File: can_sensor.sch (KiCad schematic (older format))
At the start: 53 parts, among them J1 TEST_1P, J2 TEST_1P, J3 TEST_1P, J4 TEST_1P, P1 IO1, P2 IO2, P4 CONN_01X03, P5 USB, P6 CAN_IN, P7 CAN_OUT, P8 TERM, Q1 Q_PMOS_GSD, SW1 RESET, SW2 BOOT, U1 NJM2870F0, U2 MIC5317, U3 STM32F042C6, U4 mcp2562

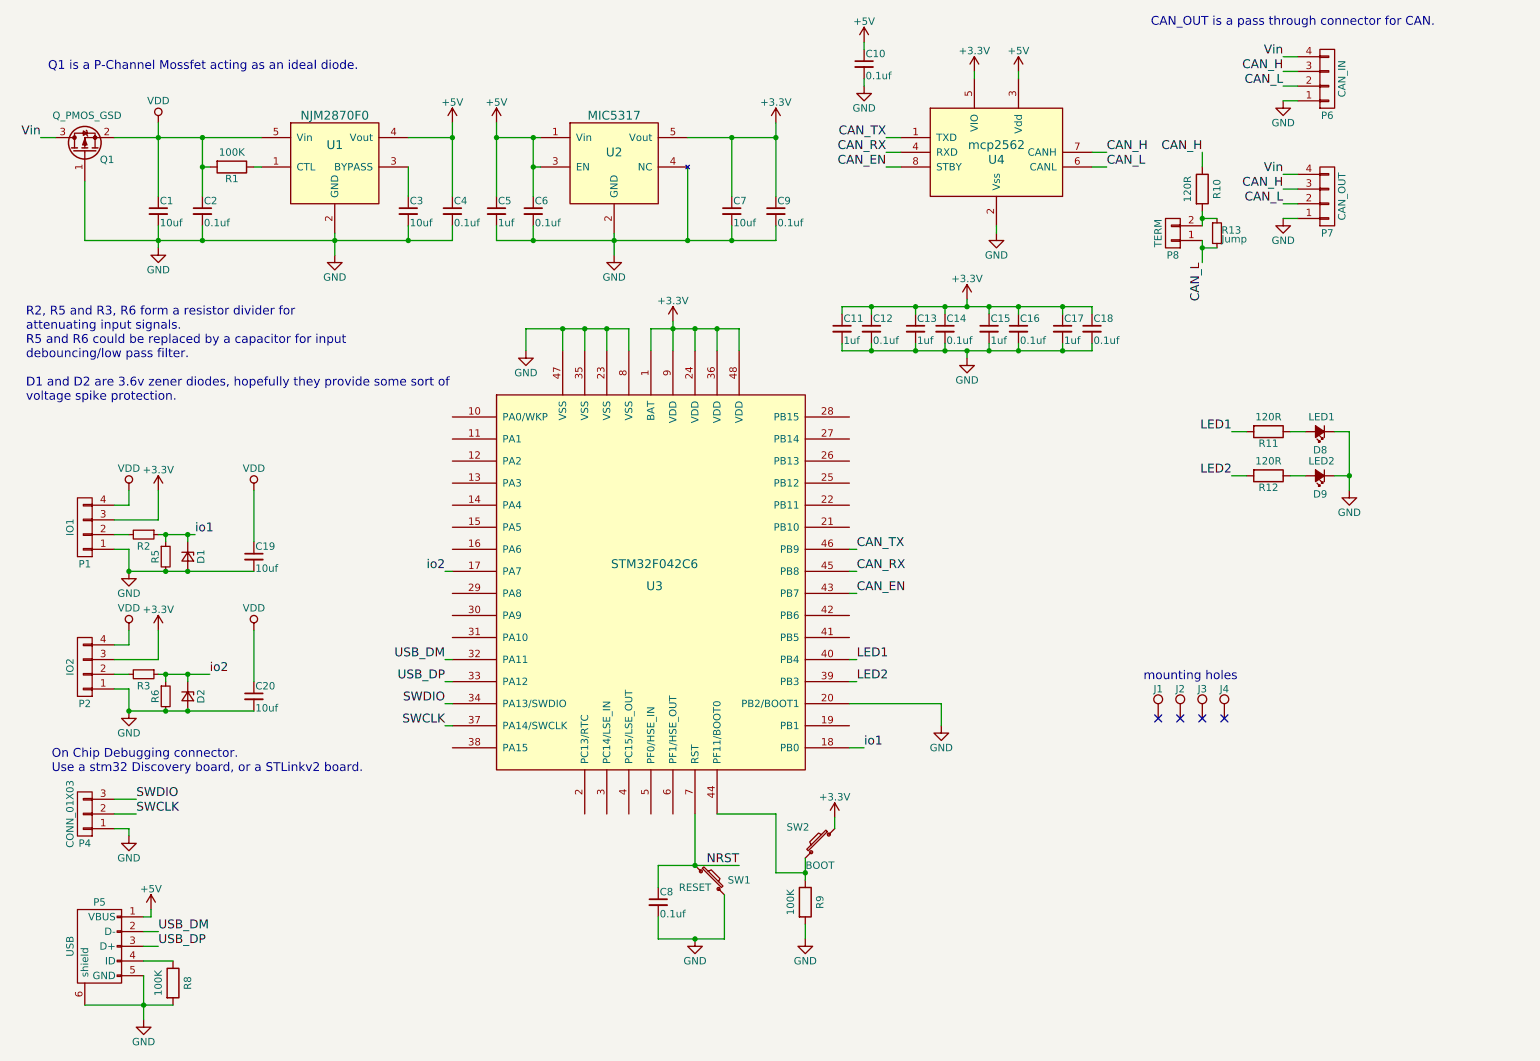
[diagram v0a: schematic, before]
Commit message: Added SPI and I2C connectors to the schematic
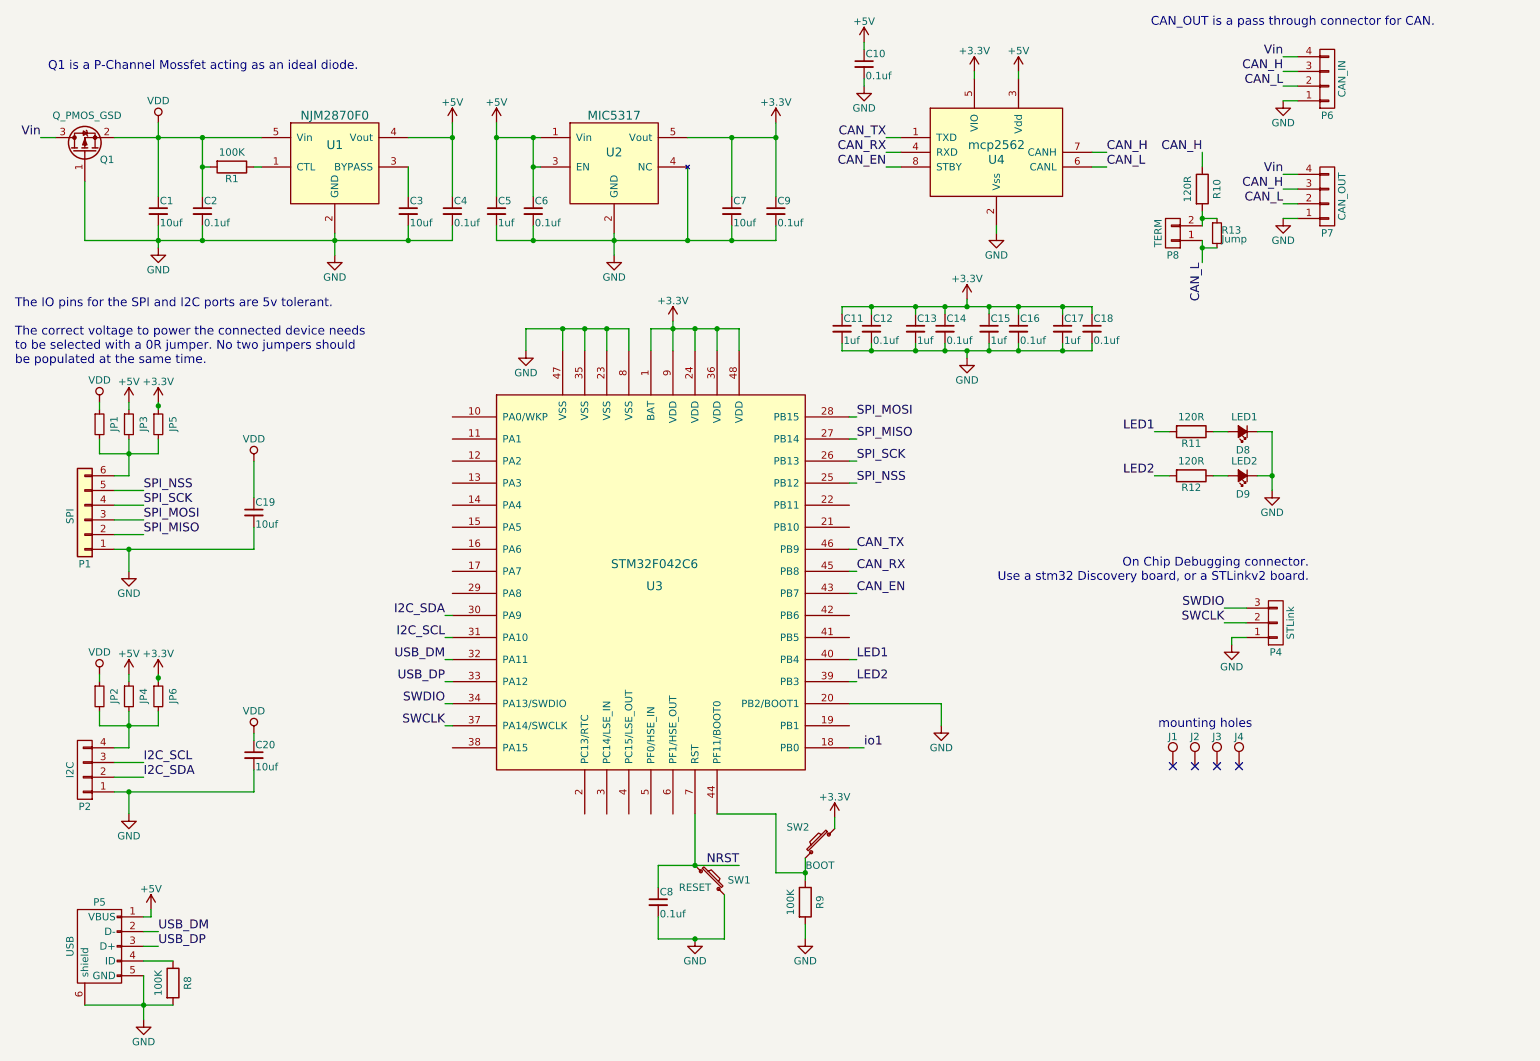
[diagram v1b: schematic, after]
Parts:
- removed D1, D2: D_Zener_Small, Diodes_SMD:D_SOD-123, symbol D_Zener_Small
- removed P1: IO1, User_Connectors:Molex-duraClick-4conn, symbol CONN_01X04
- removed R2, R3, R5, R6: R, Resistors_SMD:R_0603_HandSoldering, symbol R_Small
- added JP1, JP2: Vin, symbol R_Small
- added JP3, JP4: 3V, symbol R_Small
- added JP5, JP6: 5V, symbol R_Small
- added P1: SPI, symbol Conn_01x06
- P2: value IO2 -> I2C
- P4: value CONN_01X03 -> STLink
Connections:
- net +3V3: now also JP5.1, JP6.1; no longer P2.3 (P3)
- net +5V: now also JP3.1, JP4.1
- net GND: now also P1.1 (Pin_1)
- net VDD: now also JP1.1, JP2.1; no longer P2.4 (P4)
- net I2C_SDA: now reaches P2.2 (P2)
- net I2C_SDA: now also U3.30 (PA9)
- net SPI_NSS: now reaches U3.25 (PB12)
- net SPI_NSS: now also P1.5 (Pin_5)
- net SPI_SCK: now reaches U3.26 (PB13)
- net SPI_SCK: now also P1.4 (Pin_4)
- net SPI_MISO: now reaches U3.27 (PB14)
- net SPI_MISO: now also P1.2 (Pin_2)
- net SPI_MOSI: now reaches U3.28 (PB15)
- net SPI_MOSI: now also P1.3 (Pin_3)
- net I2C_SCL: now reaches U3.31 (PA10)
- net I2C_SCL: now also P2.3 (P3)
- net io2: no longer names the net of U3.17 (PA7)
- new net: JP2.2, JP4.2, JP6.2, P2.4 (P4)
- new net: JP1.2, JP3.2, JP5.2, P1.6 (Pin_6)
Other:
- note added: "The IO pins for the SPI and I2C ports are 5v tolerant.\n\nThe correct voltage to power the connected device needs \nto be selected with a 0R jumper. No two jumpers should \nbe populated at the same time."
- note removed: "R2, R5 and R3, R6 form a resistor divider for \nattenuating input signals.\nR5 and R6 could be replaced by a capacitor for input \ndebouncing/low pass filter.\n\nD1 and D2 are 3.6v zener diodes, hopefully they provide some sort of \nvoltage spike protection."
- moved on the sheet: C19, C20, D8, D9, J1, J2, J3, J4, P2, P4, R11, R12

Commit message: Added footprints to most components
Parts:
- D8, D9: footprint LEDs:LED_0603 -> LEDs:LED_0603_HandSoldering
- J1, J2, J3, J4: footprint (none) -> Mounting_Holes:MountingHole_3.2mm_M3_ISO7380_Pad
- JP1, JP2, JP3, JP4, JP5, JP6: footprint (none) -> Resistors_SMD:R_0603_HandSoldering

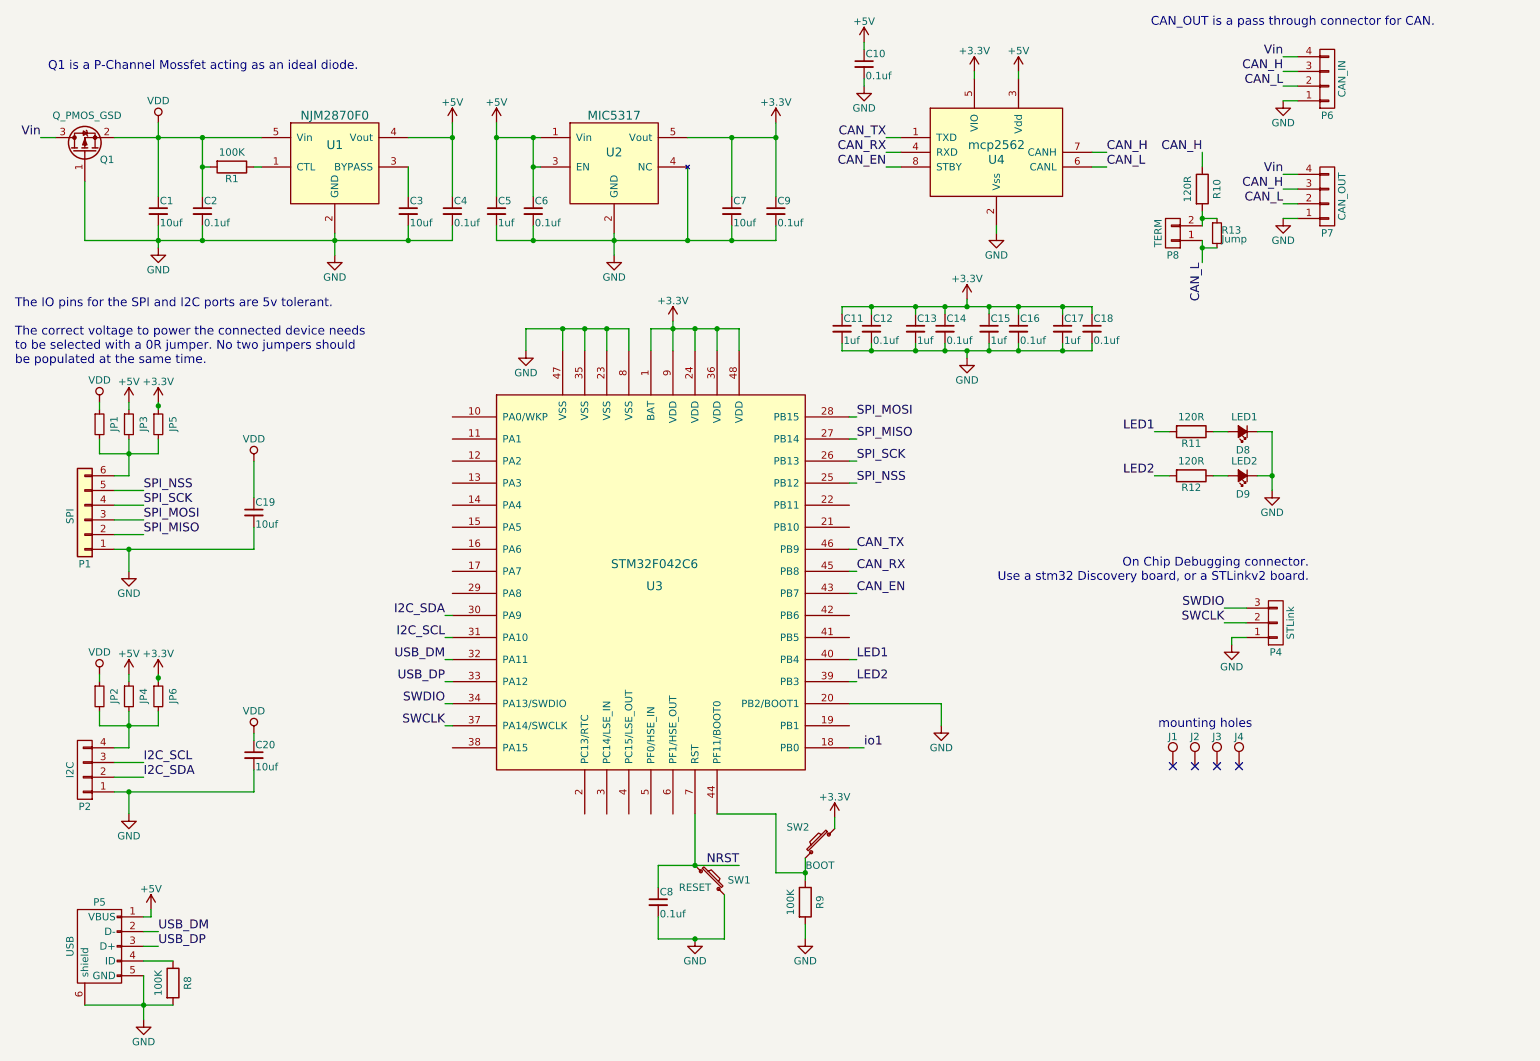
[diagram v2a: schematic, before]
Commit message: finished adding footprints & started routing
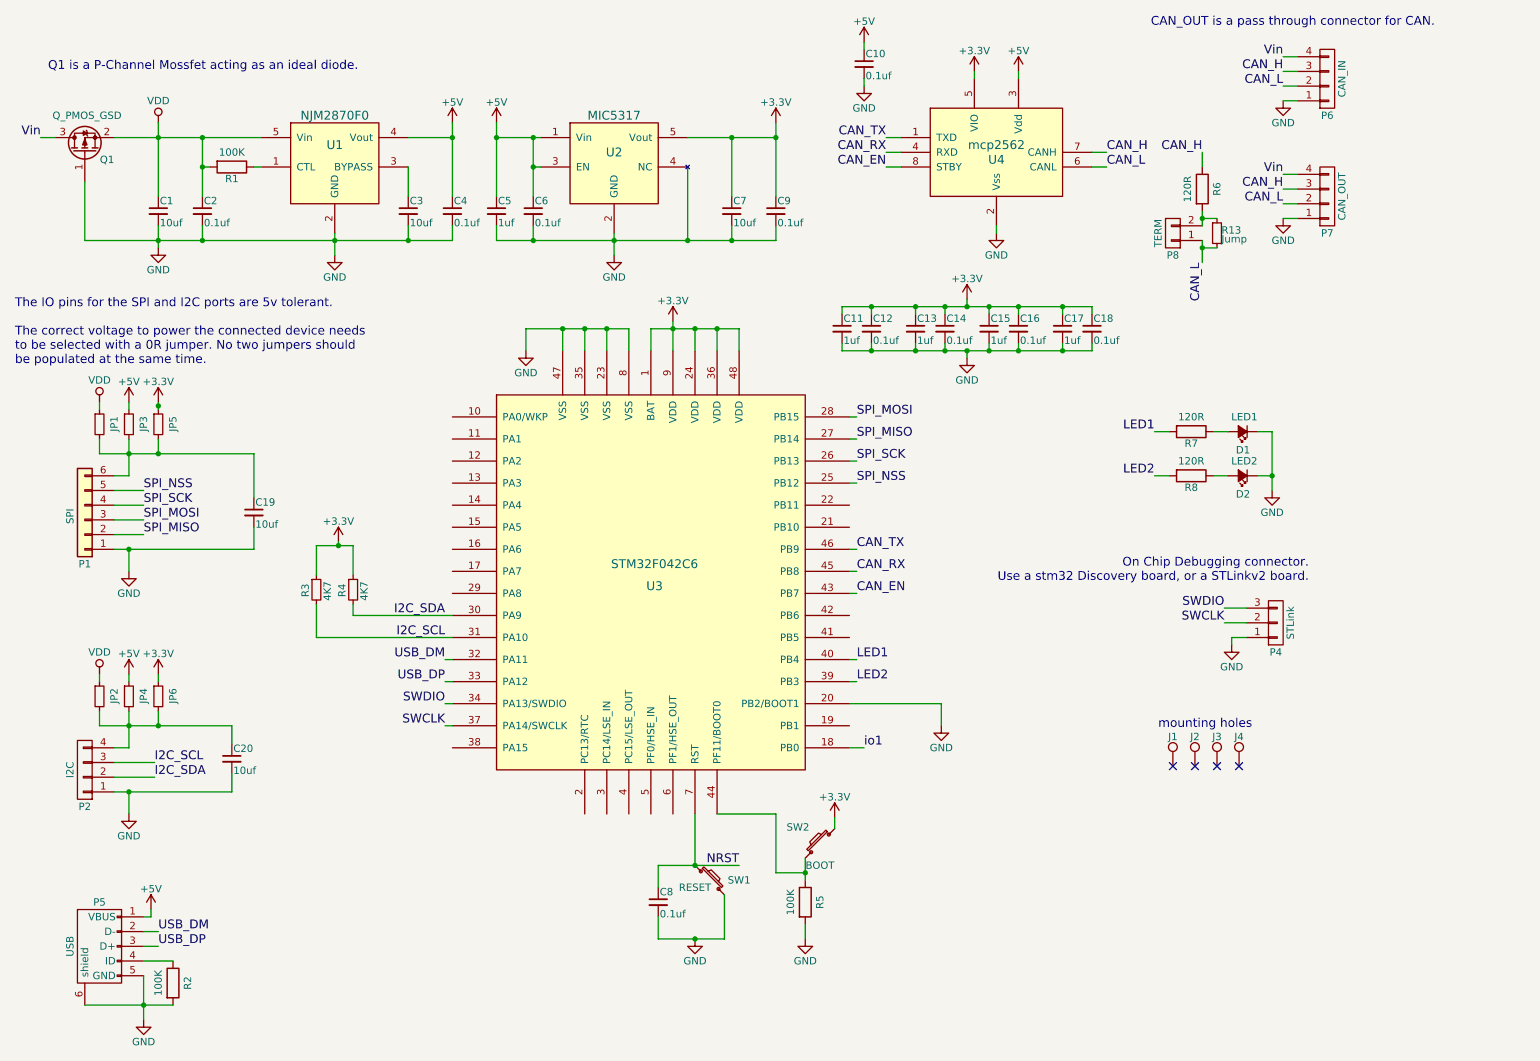
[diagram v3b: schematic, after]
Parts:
- added R3, R4: 4K7, Resistors_SMD:R_0805, symbol R_Small
- P1: footprint (none) -> Supermileage:Molex-duraClick-6conn
- renumbered D8 to D1, D9 to D2, R8 to R2, R9 to R5, R10 to R6, R11 to R7, R12 to R8
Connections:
- net +3V3: now also R3.1, R4.1
- net I2C_SCL: now also R3.2
- net I2C_SDA: now also R4.2
- net VDD: no longer C19.1, C20.1
- net at JP2.2, JP4.2, JP6.2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: now also C20.1
- net at JP1.2, JP3.2, JP5.2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: now also C19.1
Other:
- moved on the sheet: C20
